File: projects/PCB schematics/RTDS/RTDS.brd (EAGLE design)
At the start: 160 x 100 mm, 0 parts

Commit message: RTDS - Intial commit.
Board not in draft state yet. Committing out to add in parts to master.
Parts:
- added U$1: NANO, Arduino-clone:NANO
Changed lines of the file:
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@@
 </autorouter>
 <elements>
+<element name="U$1" library="Arduino-clone" package="NANO" value="NANO" x="-7.62" y="11.43" smashed="yes"/>
 </elements>
 <signals>

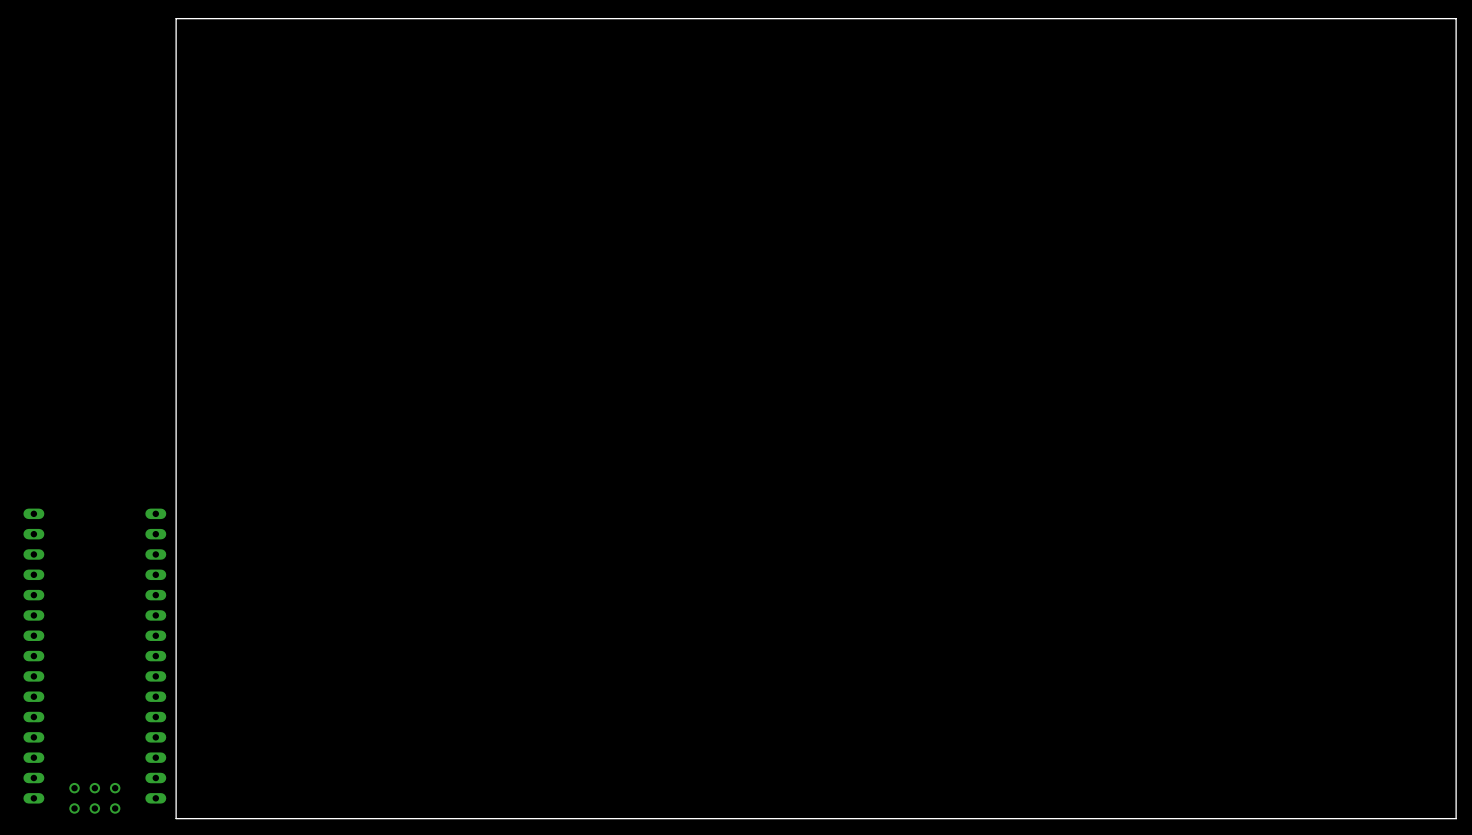
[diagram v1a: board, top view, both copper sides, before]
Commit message: RTDS - Initial draft.
Arduino Nano and SoundFX boards added.
Must complete wiring.
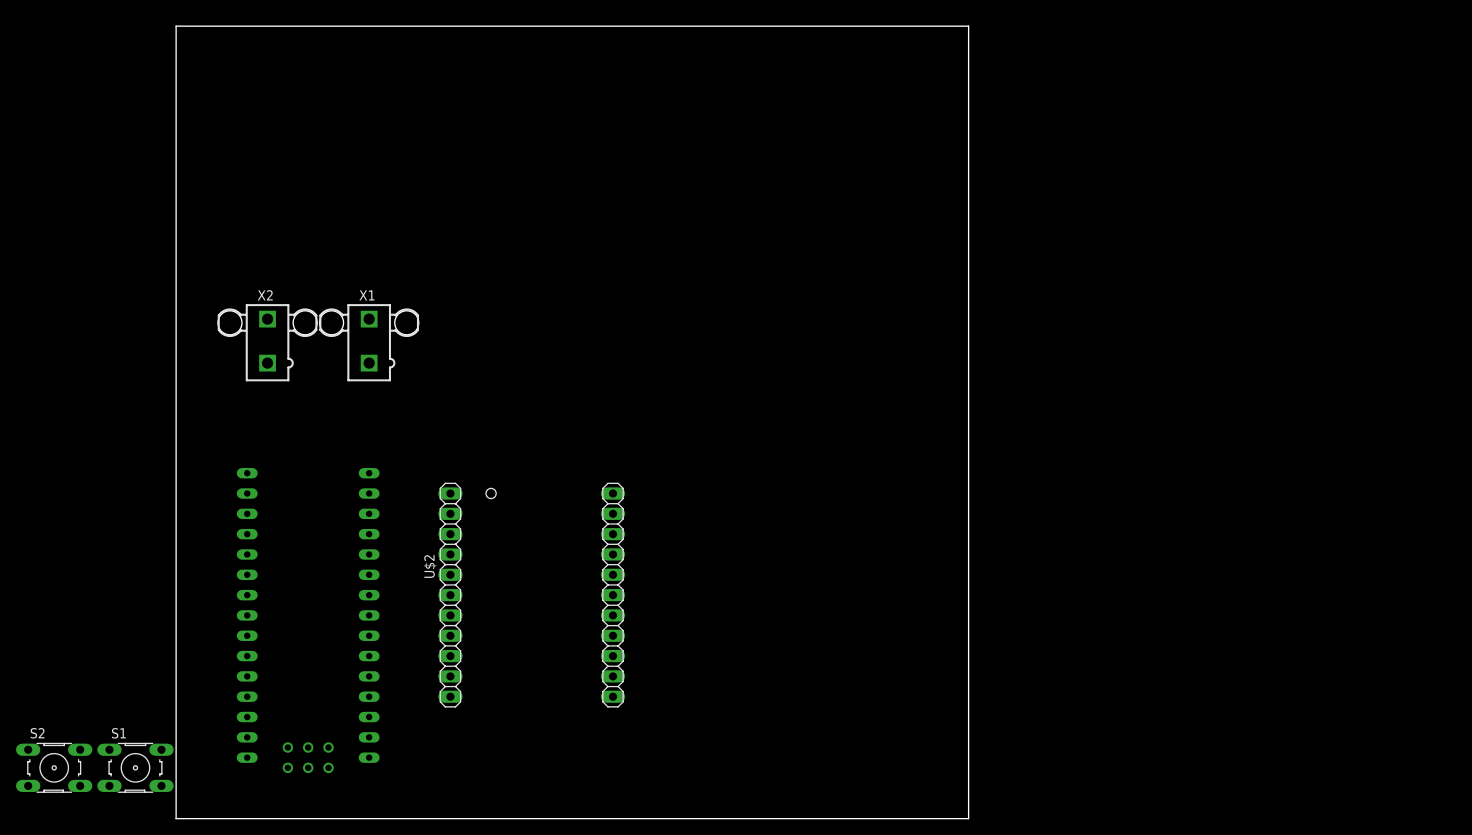
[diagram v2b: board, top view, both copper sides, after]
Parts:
- added S1, S2: (no value), switch-omron:B3F-10XX
- added U$2: ADA-SOUNDFX, IowaFormula:ADA-SOUNDFX
- added X1, X2: 5566-2, con-molex:5566-2
- moved U$1 27.1 mm to (19.1, 16.5)
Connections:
- new net GND: U$1.GND, U$1.GND1, U$2.11, U$2.12, U$2.15, U$2.21, X2.1, X2.2
- new net VCC: U$1.RAW, X1.1, X1.2
- new net VIN: U$1.5V, U$2.22
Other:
- board size 160 x 100 mm -> 99.1 x 99.1 mm

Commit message: RTDS - Rev A.
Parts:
- removed S1, S2: (no value), switch-omron:B3F-10XX
- added R1, R2: 47k, rcl:R0805
- added SH1: SHORTT5, shorts:SHORT_TOP-50
- added U$3: MAX9744, IowaFormula:MAX9744
- added X3, X4, X5: 5566-2, con-molex:5566-2
- U$1: value NANO -> MAX9744; device Arduino-clone:NANO -> IowaFormula:MAX9744
- moved U$2 76.3 mm to (87.6, 69.8), turned to 90 degrees
- moved U$1 58.5 mm to (57.1, 61.0), turned to 270 degrees
- moved X2 23.4 mm to (29.2, 74.9)
- moved X1 18.3 mm to (14.0, 74.9)
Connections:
- new net +12V-ISO: X1.1, X1.2, X2.1, X2.2
- new net AUDIO_GND: U$1.AGND, U$2.12, U$3.AGND
- new net LEFT: U$2.13
- new net N$1: U$1.GND
- new net RESET_SIGNAL: R2.2, U$2.1
- new net RIGHT: U$2.14
- new net RTDS_SIGNAL: R1.2, U$2.2, X5.1, X5.2
- net GND: now also U$3.GND, X4.1, X4.2; no longer U$1.GND, U$1.GND1, U$2.12, X2.1, X2.2
- net VCC: now also R1.1, R2.1, SH1.2, X3.1, X3.2; no longer U$1.RAW, X1.1, X1.2
- net VIN: now also SH1.1; no longer U$1.5V
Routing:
- net AUDIO_GND: track 0.00 -> 143.9 mm
- net RTDS_SIGNAL: track 0.00 -> 72.3 mm, vias 0 -> 1
- net VCC: track 0.00 -> 71.3 mm, vias 0 -> 2
- net +12V-ISO: track 0.00 -> 42.9 mm
- net RESET_SIGNAL: track 0.00 -> 13.5 mm
- net VIN: track 0.00 -> 3.70 mm
- added copper zone on layer 1, net GND
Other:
- board text added: "Author: github.com/michaelpass"
- board text added: "I/O: 1. +12V-ISO (X1) 2. +12V-ISO (X2) 3. VCC (X3) 4. GND (X4) 5. RTDS_SIGNAL (X5)"
- board text added: "Rready-To-Drive Sound (RTDS) Board Rev A: 04/30/19"

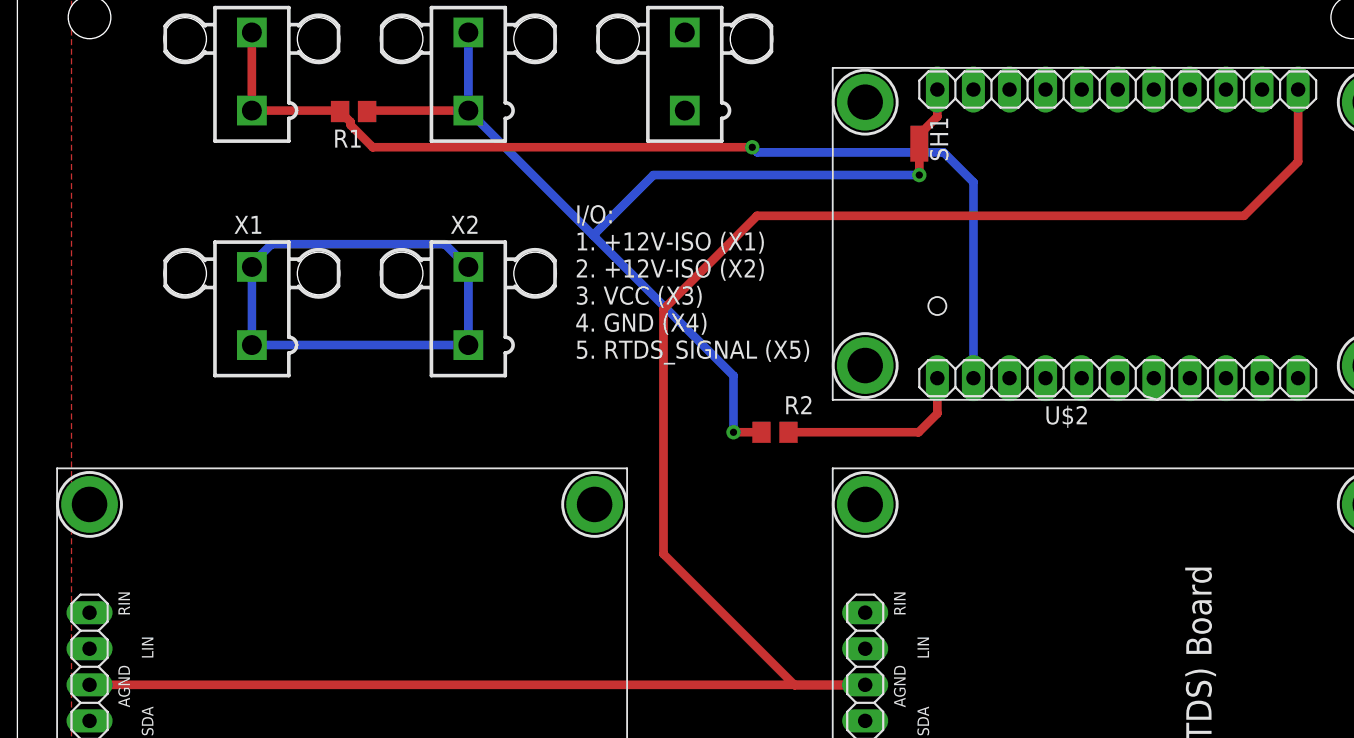
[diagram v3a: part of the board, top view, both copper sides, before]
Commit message: RTDS - R L audio wiring to amplifiers.
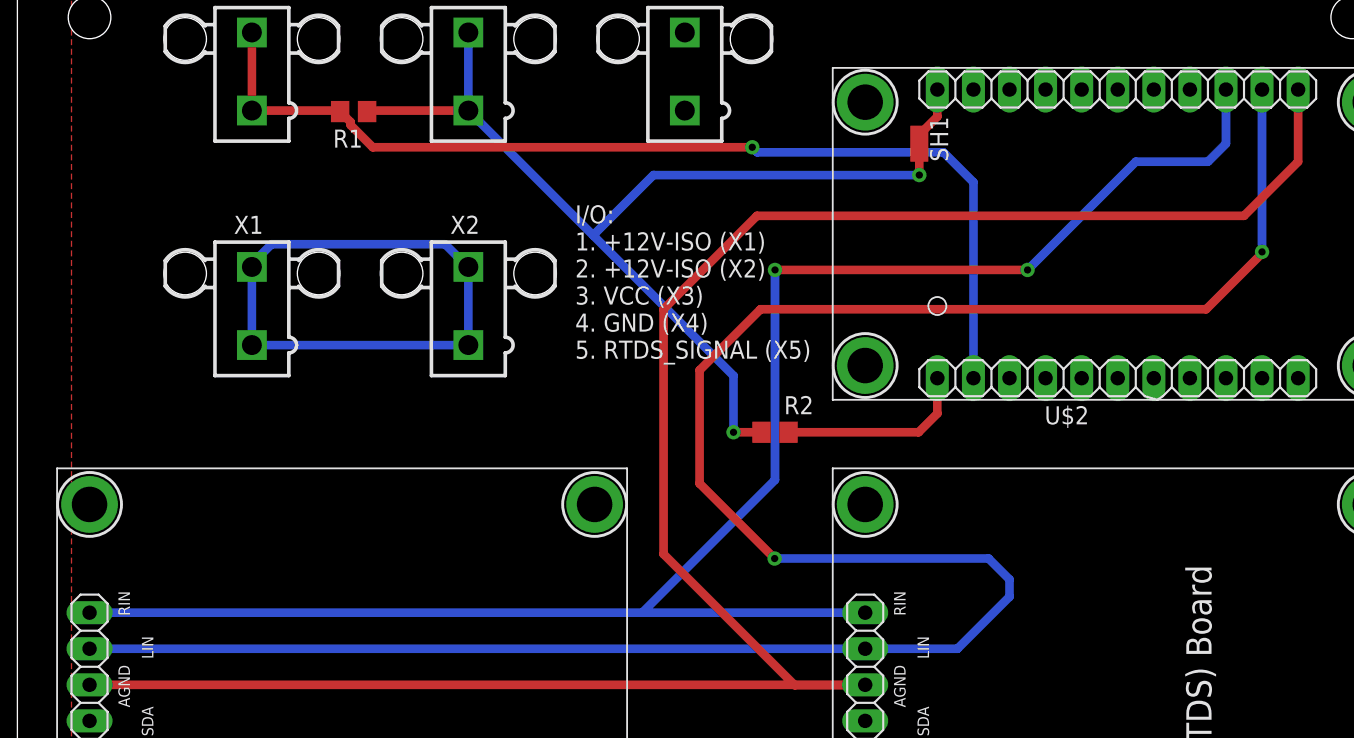
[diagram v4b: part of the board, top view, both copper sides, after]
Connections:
- net LEFT: now also U$1.LIN, U$3.LIN
- net RIGHT: now also U$1.RIN, U$3.RIN
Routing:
- net LEFT: track 0.00 -> 154.7 mm, vias 0 -> 2
- net RIGHT: track 0.00 -> 121.9 mm, vias 0 -> 2
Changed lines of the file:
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@@
 <signal name="RIGHT">
 <contactref element="U$2" pad="14"/>
+<contactref element="U$1" pad="RIN"/>
+<contactref element="U$3" pad="RIN"/>
+<wire x1="2.54" y1="53.34" x2="41.4528" y2="53.34" width="0.6096" layer="16"/>
+<wire x1="41.4528" y1="53.34" x2="50.8" y2="62.6872" width="0.6096" layer="16"/>
+<wire x1="50.8" y1="62.6872" x2="50.8" y2="77.47" width="0.6096" layer="16"/>
+<via x="50.8" y="77.47" extent="1-16" drill="0.508"/>
+<wire x1="50.8" y1="77.47" x2="68.58" y2="77.47" width="0.6096" layer="1"/>
+<via x="68.58" y="77.47" extent="1-16" drill="0.508"/>
+<wire x1="68.58" y1="77.47" x2="76.2" y2="85.09" width="0.6096" layer="16"/>
+<wire x1="76.2" y1="85.09" x2="81.28" y2="85.09" width="0.6096" layer="16"/>
+<wire x1="81.28" y1="85.09" x2="82.55" y2="86.36" width="0.6096" layer="16"/>
+<wire x1="82.55" y1="86.36" x2="82.55" y2="90.17" width="0.6096" layer="16"/>
+<wire x1="41.4528" y1="53.34" x2="57.15" y2="53.34" width="0.6096" layer="16"/>
 </signal>
 <signal name="LEFT">
 <contactref element="U$2" pad="13"/>
+<contactref element="U$1" pad="LIN"/>
+<contactref element="U$3" pad="LIN"/>
+<wire x1="57.15" y1="50.8" x2="2.54" y2="50.8" width="0.6096" layer="16"/>
+<wire x1="57.15" y1="50.8" x2="63.6524" y2="50.8" width="0.6096" layer="16"/>
+<wire x1="63.6524" y1="50.8" x2="67.31" y2="54.4576" width="0.6096" layer="16"/>
+<wire x1="65.8368" y1="57.15" x2="50.7746" y2="57.15" width="0.6096" layer="16"/>
+<via x="50.7746" y="57.15" extent="1-16" drill="0.508"/>
+<wire x1="50.7746" y1="57.15" x2="45.4914" y2="62.4332" width="0.6096" layer="1"/>
+<wire x1="45.4914" y1="62.4332" x2="45.4914" y2="70.4088" width="0.6096" layer="1"/>
+<wire x1="45.4914" y1="70.4088" x2="49.784" y2="74.7014" width="0.6096" layer="1"/>
+<wire x1="81.153" y1="74.7014" x2="85.1408" y2="78.6892" width="0.6096" layer="1"/>
+<wire x1="85.1408" y1="78.6892" x2="85.09" y2="78.74" width="0.6096" layer="1"/>
+<via x="85.09" y="78.74" extent="1-16" drill="0.508"/>
+<wire x1="85.09" y1="78.74" x2="85.09" y2="90.17" width="0.6096" layer="16"/>
+<wire x1="67.31" y1="54.4576" x2="67.31" y2="55.6768" width="0.6096" layer="16"/>
+<wire x1="67.31" y1="55.6768" x2="65.8368" y2="57.15" width="0.6096" layer="16"/>
+<wire x1="49.784" y1="74.7014" x2="81.153" y2="74.7014" width="0.6096" layer="1"/>
 </signal>
 <signal name="AUDIO_GND">
